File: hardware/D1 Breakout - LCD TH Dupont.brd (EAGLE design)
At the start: 51.7 x 45.7 mm, 10 parts, among them J1 RJ11-4L-B

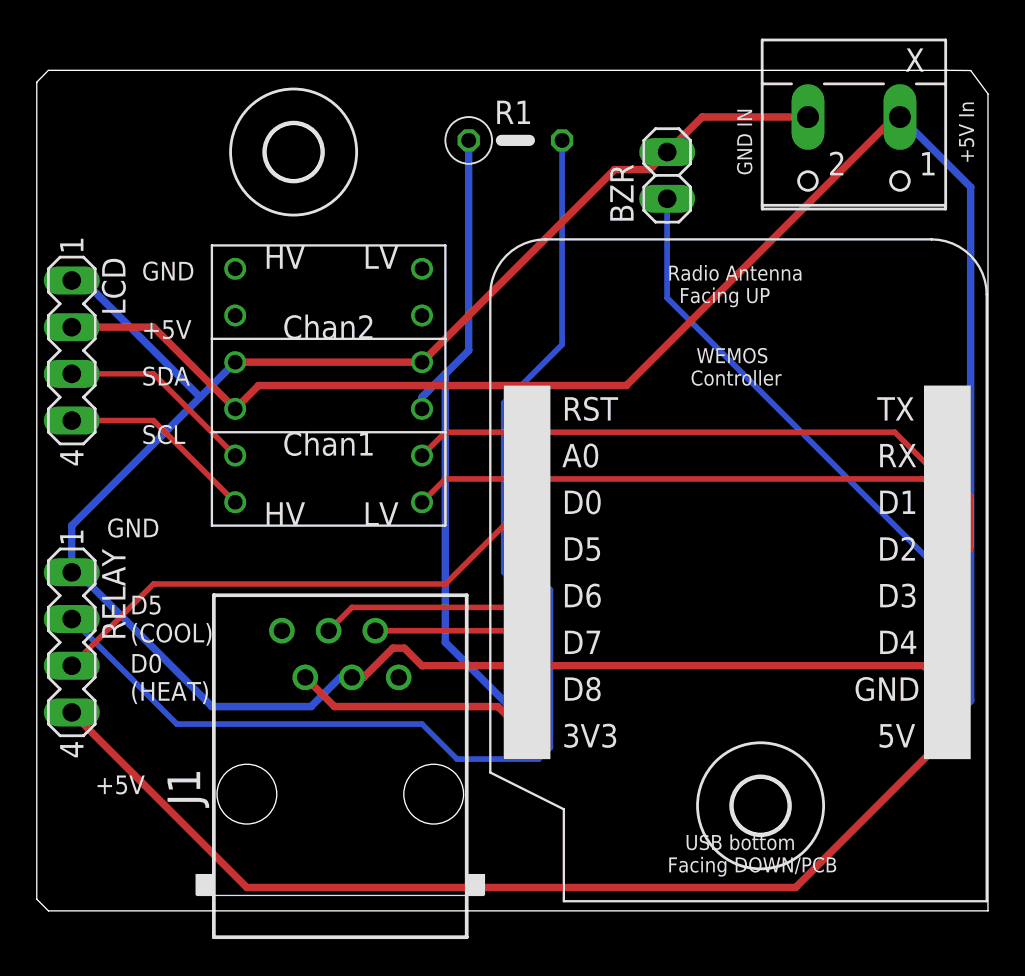
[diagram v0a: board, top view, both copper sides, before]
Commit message: Change level shifter to most recent version
- move from https://www.sparkfun.com/products/retired/8745
  to https://www.sparkfun.com/products/12009
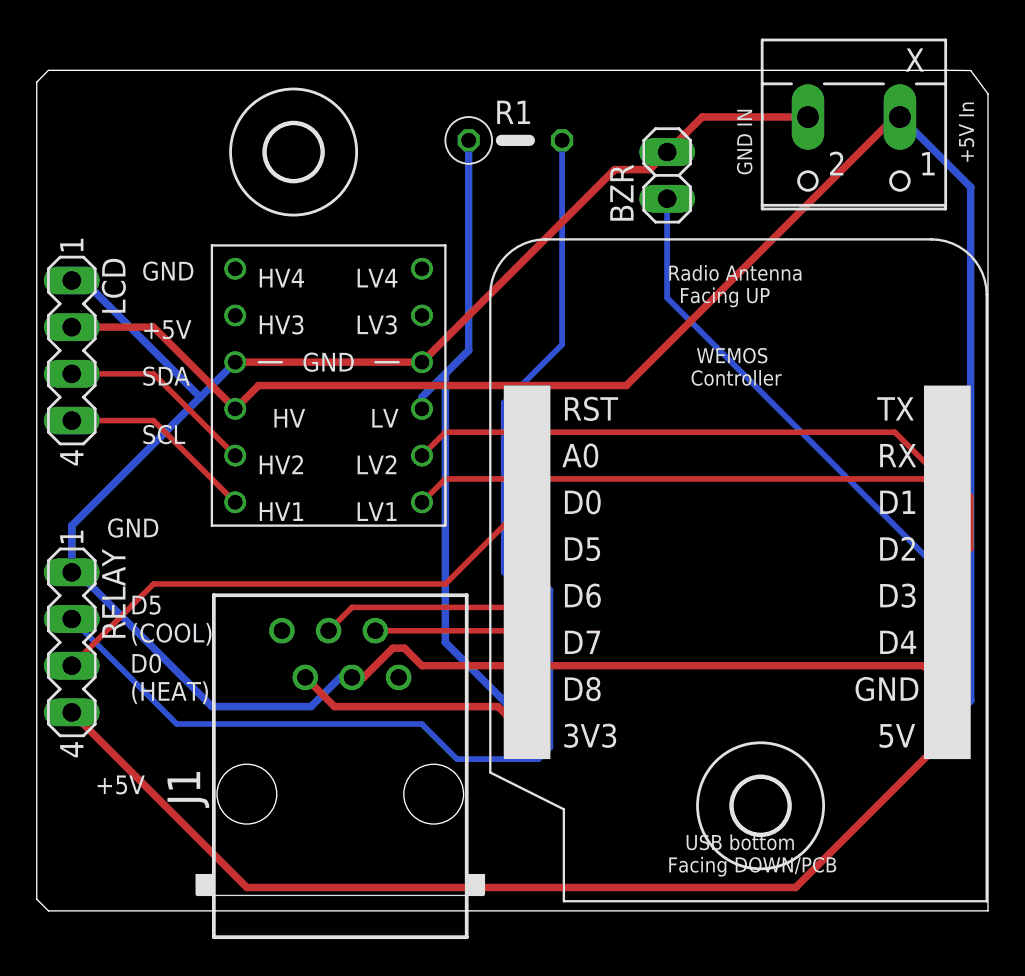
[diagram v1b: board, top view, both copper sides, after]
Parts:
- U$3: value LOGIC_LEVEL_CONVERTER -> SPARKFUN-BOARDS_LOGIC_LEVEL_CONVERTER; device SparkFun-Boards:LOGIC_LEVEL_CONVERTER -> D1 Breakout - LCD TH Dupont:SPARKFUN-BOARDS_LOGIC_LEVEL_CONVERTER
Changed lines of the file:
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@@
 <?xml version="1.0" encoding="utf-8"?>
 <!DOCTYPE eagle SYSTEM "eagle.dtd">
-<eagle version="7.3.0">
+<eagle version="7.7.0">
 <drawing>
 <settings>
@@
 <layer number="59" name="tCarbon" color="7" fill="1" visible="no" active="no"/>
 <layer number="60" name="bCarbon" color="7" fill="1" visible="no" active="no"/>
+<layer number="88" name="SimResults" color="9" fill="1" visible="no" active="no"/>
+<layer number="89" name="SimProbes" color="9" fill="1" visible="no" active="no"/>
 <layer number="90" name="Modules" color="5" fill="1" visible="no" active="no"/>
 <layer number="91" name="Nets" color="2" fill="1" visible="no" active="no"/>
@@
 <param name="dpMaxLengthDifference" value="10mm"/>
 <param name="dpGapFactor" value="2.5"/>
-<param name="checkGrid" value="0"/>
 <param name="checkAngle" value="0"/>
 <param name="checkFont" value="1"/>
 <param name="checkRestrict" value="1"/>
+<param name="checkStop" value="0"/>
+<param name="checkValues" value="0"/>
+<param name="checkNames" value="1"/>
+<param name="checkWireStubs" value="1"/>
+<param name="checkPolygonWidth" value="0"/>
 <param name="useDiameter" value="13"/>
 <param name="maxErrors" value="50"/>
@@
 </autorouter>
 <elements>
-<element name="U$1" library="1455413453956-wemos" package="WEMOS" value="WEMOS" x="58.42" y="38.1"/>
+<element name="U$1" library="1455413453956-wemos" package="WEMOS" value="WEMOS" x="58.42" y="38.1" smashed="yes"/>
 <element name="X" library="con-wago-500" package="W237-102" value="PWR" x="76.2" y="70.485" smashed="yes" rot="R180">
 <attribute name="MF" value="" x="76.2" y="70.485" size="0.8128" layer="27" rot="R180" display="off"/>
 <attribute name="MPN" value="237-102" x="76.2" y="70.485" size="0.8128" layer="27" rot="R180" display="off"/>
+<attribute name="NAME" x="80.0462" y="75.4888" size="1.27" layer="25" ratio="10" rot="R180"/>
+<attribute name="OC_FARNELL" value="unknown" x="76.2" y="70.485" size="0.8128" layer="27" rot="R180" display="off"/>
 <attribute name="OC_NEWARK" value="70K9898" x="76.2" y="70.485" size="0.8128" layer="27" rot="R180" display="off"/>
-<attribute name="OC_FARNELL" value="unknown" x="76.2" y="70.485" size="0.8128" layer="27" rot="R180" display="off"/>
 <attribute name="VALUE" x="73.7" y="64.77" size="1.27" layer="27" ratio="10"/>
-<attribute name="NAME" x="80.0462" y="75.4888" size="1.27" layer="25" ratio="10" rot="R180"/>
 </element>
-<element name="J1" library="con-tycoelectronics" package="RJ11-NO_SHIELD" value="RJ11-4L-B" x="48.26" y="34.925">
+<element name="J1" library="con-tycoelectronics" package="RJ11-NO_SHIELD" value="RJ11-4L-B" x="48.26" y="34.925" smashed="yes">
 <attribute name="MF" value="TYCO ELECTRONICS" x="48.26" y="34.925" size="1.778" layer="27" display="off"/>
+<attribute name="MPN" value="RJ11-4L-B" x="48.26" y="34.925" size="1.778" layer="27" display="off"/>
+<attribute name="NAME" x="40.64" y="34.29" size="1.778" layer="25" rot="R90"/>
+<attribute name="OC_FARNELL" value="unknown" x="48.26" y="34.925" size="1.778" layer="27" display="off"/>
 <attribute name="OC_NEWARK" value="52K3315" x="48.26" y="34.925" size="1.778" layer="27" display="off"/>
-<attribute name="MPN" value="RJ11-4L-B" x="48.26" y="34.925" size="1.778" layer="27" display="off"/>
-<attribute name="OC_FARNELL" value="unknown" x="48.26" y="34.925" size="1.778" layer="27" display="off"/>
+<attribute name="VALUE" x="42.545" y="37.465" size="1.778" layer="27"/>
 </element>
-<element name="R1" library="rcl" package="0207/5V" value="10k" x="57.785" y="70.485"/>
-<element name="U$2" library="holes" package="3,0" value="" x="45.72" y="69.85"/>
-<element name="U$4" library="holes" package="3,0" value="" x="71.12" y="34.29"/>
-<element name="U$3" library="SparkFun-Boards" package="LOGIC_LEVEL_CONVERTER" value="LOGIC_LEVEL_CONVERTER" x="53.975" y="64.77" rot="R180"/>
-<element name="BZR" library="pinhead" package="1X02" value="" x="66.04" y="68.58" rot="R90"/>
-<element name="RELAY" library="con-lstb" package="MA04-1" value="" x="33.655" y="43.18" rot="R270">
+<element name="R1" library="rcl" package="0207/5V" value="10k" x="57.785" y="70.485" smashed="yes">
+<attribute name="NAME" x="56.642" y="71.374" size="1.27" layer="25" ratio="10"/>
+<attribute name="VALUE" x="56.642" y="68.326" size="1.27" layer="27" ratio="10"/>
+</element>
+<element name="U$2" library="holes" package="3,0" value="" x="45.72" y="69.85" smashed="yes"/>
+<element name="U$4" library="holes" package="3,0" value="" x="71.12" y="34.29" smashed="yes"/>
+<element name="U$3" library="D1 Breakout - LCD TH Dupont" package="SPARKFUN-BOARDS_LOGIC_LEVEL_CONVERTER" value="SPARKFUN-BOARDS_LOGIC_LEVEL_CONVERTER" x="53.975" y="64.77" smashed="yes" rot="R180"/>
+<element name="BZR" library="pinhead" package="1X02" value="" x="66.04" y="68.58" smashed="yes" rot="R90">
+<attribute name="NAME" x="64.2112" y="65.9638" size="1.27" layer="25" ratio="10" rot="R90"/>
+<attribute name="VALUE" x="69.215" y="66.04" size="1.27" layer="27" rot="R90"/>
+</element>
+<element name="RELAY" library="con-lstb" package="MA04-1" value="" x="33.655" y="43.18" smashed="yes" rot="R270">
 <attribute name="MF" value="" x="33.655" y="43.18" size="1.778" layer="27" rot="R270" display="off"/>
+<attribute name="MPN" value="" x="33.655" y="43.18" size="1.778" layer="27" rot="R270" display="off"/>
+<attribute name="NAME" x="35.306" y="48.26" size="1.27" layer="25" ratio="10" rot="R270"/>
+<attribute name="OC_FARNELL" value="unknown" x="33.655" y="43.18" size="1.778" layer="27" rot="R270" display="off"/>
 <attribute name="OC_NEWARK" value="unknown" x="33.655" y="43.18" size="1.778" layer="27" rot="R270" display="off"/>
-<attribute name="OC_FARNELL" value="unknown" x="33.655" y="43.18" size="1.778" layer="27" rot="R270" display="off"/>
-<attribute name="MPN" value="" x="33.655" y="43.18" size="1.778" layer="27" rot="R270" display="off"/>
+<attribute name="VALUE" x="35.306" y="42.545" size="1.27" layer="27" ratio="10" rot="R270"/>
 </element>
-<element name="LCD" library="con-lstb" package="MA04-1" value="" x="33.655" y="59.055" rot="R270">
+<element name="LCD" library="con-lstb" package="MA04-1" value="" x="33.655" y="59.055" smashed="yes" rot="R270">
 <attribute name="MF" value="" x="33.655" y="59.055" size="1.778" layer="27" rot="R270" display="off"/>
+<attribute name="MPN" value="" x="33.655" y="59.055" size="1.778" layer="27" rot="R270" display="off"/>
+<attribute name="NAME" x="35.306" y="64.135" size="1.27" layer="25" ratio="10" rot="R270"/>
+<attribute name="OC_FARNELL" value="unknown" x="33.655" y="59.055" size="1.778" layer="27" rot="R270" display="off"/>
 <attribute name="OC_NEWARK" value="unknown" x="33.655" y="59.055" size="1.778" layer="27" rot="R270" display="off"/>
-<attribute name="OC_FARNELL" value="unknown" x="33.655" y="59.055" size="1.778" layer="27" rot="R270" display="off"/>
-<attribute name="MPN" value="" x="33.655" y="59.055" size="1.778" layer="27" rot="R270" display="off"/>
+<attribute name="VALUE" x="35.306" y="58.42" size="1.27" layer="27" ratio="10" rot="R270"/>
 </element>
 </elements>
@@
 </signal>
 </signals>
+<mfgpreviewcolors>
+<mfgpreviewcolor name="soldermaskcolor" color="0xC8008000"/>
+<mfgpreviewcolor name="silkscreencolor" color="0xFFFEFEFE"/>
+<mfgpreviewcolor name="backgroundcolor" color="0xFF282828"/>
+<mfgpreviewcolor name="coppercolor" color="0xFFFFBF00"/>
+<mfgpreviewcolor name="substratecolor" color="0xFF786E46"/>
+</mfgpreviewcolors>
 </board>
 </drawing>
